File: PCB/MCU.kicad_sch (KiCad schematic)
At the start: 27 parts, among them J1 SWD, SW65 Settings, SW66 Reset, U2 W25Q128JVS, U3 RP2040, Y1 12MHz

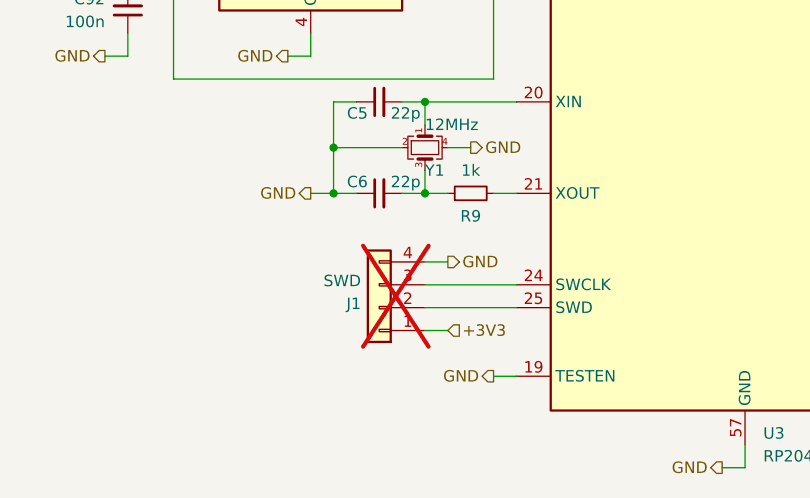
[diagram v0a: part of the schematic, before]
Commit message: Changed RGB LED voltage to 5V.
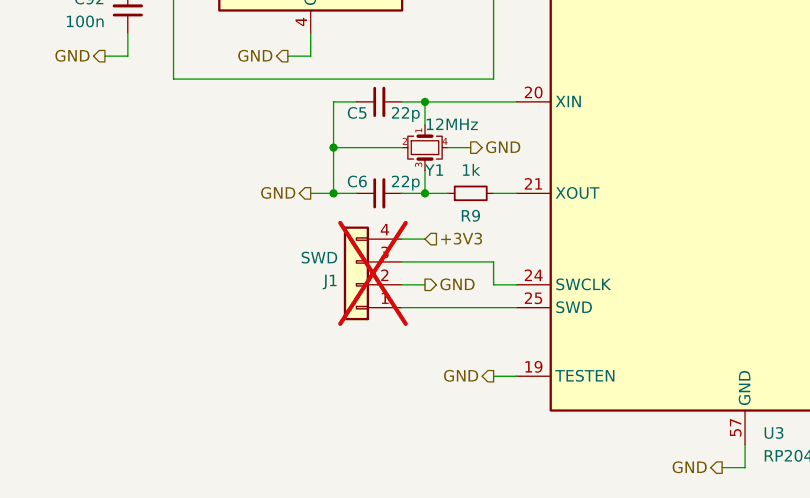
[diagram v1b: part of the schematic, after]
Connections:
- net +3V3: now also J1.4 (Pin_4); no longer J1.1 (Pin_1)
- net GND: now also J1.2 (Pin_2); no longer J1.4 (Pin_4)
- net at U3.25 (SWD): now also J1.1 (Pin_1); no longer J1.2 (Pin_2)
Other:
- moved on the sheet: J1
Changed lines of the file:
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@@
+    (stroke (width 0) (type default))
+  )
+  (wire (pts (xy 66.04 100.33) (xy 68.58 100.33))
     (stroke (width 0) (type default))
   )
@@
     (stroke (width 0) (type default))
   )
+  (wire (pts (xy 66.04 97.79) (xy 66.04 100.33))
+    (stroke (width 0) (type default))
+  )
   (wire (pts (xy 167.64 16.51) (xy 177.8 16.51))
     (stroke (width 0) (type default))
@@
     (stroke (width 0) (type default))
   )
-  (wire (pts (xy 58.42 100.33) (xy 68.58 100.33))
-    (stroke (width 0) (type default))
-  )
   (wire (pts (xy 116.84 26.67) (xy 106.68 26.67))
     (stroke (width 0) (type default))
@@
     (stroke (width 0) (type default))
   )
+  (wire (pts (xy 55.88 97.79) (xy 66.04 97.79))
+    (stroke (width 0) (type default))
+  )
   (wire (pts (xy 106.68 16.51) (xy 116.84 16.51))
     (stroke (width 0) (type default))
@@
     (stroke (width 0) (type default))
   )
-  (wire (pts (xy 60.96 97.79) (xy 58.42 97.79))
+  (wire (pts (xy 58.42 100.33) (xy 55.88 100.33))
     (stroke (width 0) (type default))
   )
@@
     (stroke (width 0) (type default))
   )
-  (wire (pts (xy 58.42 102.87) (xy 68.58 102.87))
+  (wire (pts (xy 55.88 102.87) (xy 68.58 102.87))
     (stroke (width 0) (type default))
   )
@@
     (stroke (width 0) (type default))
   )
-  (wire (pts (xy 60.96 105.41) (xy 58.42 105.41))
+  (wire (pts (xy 58.42 95.25) (xy 55.88 95.25))
     (stroke (width 0) (type default))
   )
@@
     (effects (font (size 1.27 1.27)) (justify right))
   )
-  (hierarchical_label "+3V3" (shape input) (at 60.96 105.41 0) (fields_autoplaced)
+  (hierarchical_label "+3V3" (shape input) (at 58.42 95.25 0) (fields_autoplaced)
     (effects (font (size 1.27 1.27)) (justify left))
   )
@@
     (effects (font (size 1.27 1.27)) (justify right))
   )
-  (hierarchical_label "GND" (shape output) (at 60.96 97.79 0) (fields_autoplaced)
+  (hierarchical_label "GND" (shape output) (at 58.42 100.33 0) (fields_autoplaced)
     (effects (font (size 1.27 1.27)) (justify left))
   )
@@
     )
   )
-  (symbol (lib_id "Connector_Generic:Conn_01x04") (at 53.34 102.87 180) (unit 1)
-    (in_bom no) (on_board yes) (dnp yes) (fields_autoplaced)
-    (property "Reference" "J1" (at 51.308 102.4347 0)
+  (symbol (lib_id "Connector_Generic:Conn_01x04") (at 50.8 100.33 180) (unit 1)
+    (in_bom no) (on_board yes) (dnp yes)
+    (property "Reference" "J1" (at 48.768 99.8947 0)
       (effects (font (size 1.27 1.27)) (justify left))
     )
-    (property "Value" "SWD" (at 51.308 99.8978 0)
+    (property "Value" "SWD" (at 48.768 97.3578 0)
       (effects (font (size 1.27 1.27)) (justify left))
     )
-    (property "Footprint" "Connector_PinHeader_2.54mm:PinHeader_1x04_P2.54mm_Vertical" (at 53.34 102.87 0)
-      (effects (font (size 1.27 1.27)) hide)
-    )
-    (property "Datasheet" "~" (at 53.34 102.87 0)
-      (effects (font (size 1.27 1.27)) hide)
-    )
-    (property "Description" "Debug header" (at 53.34 102.87 0)
-      (effects (font (size 1.27 1.27)) hide)
-    )
+    (property "Footprint" "Connector_PinHeader_2.54mm:PinHeader_1x04_P2.54mm_Vertical" (at 50.8 100.33 0)
+      (effects (font (size 1.27 1.27)) hide)
+    )
+    (property "Datasheet" "~" (at 50.8 100.33 0)
+      (effects (font (size 1.27 1.27)) hide)
+    )
+    (property "Description" "Debug header" (at 50.8 100.33 0)
+      (effects (font (size 1.27 1.27)) hide)
+    )

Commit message: Massive mistake corrections and clarifications.
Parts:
- added R10: 10k, Resistor_SMD:R_0402_1005Metric, symbol Device:R_Small
- R7, R8: value 22 -> 27; LCSC part number C25092 -> C25100
- SW65: value Settings -> USB Boot
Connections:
- net +3V3: now also R10.2
- net at SW66.2 (B), U3.26 (RUN): now also R10.1
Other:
- moved on the sheet: C10, C11, C12, C13, C14, C15, C16, C17, C18, C19, C5, C6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

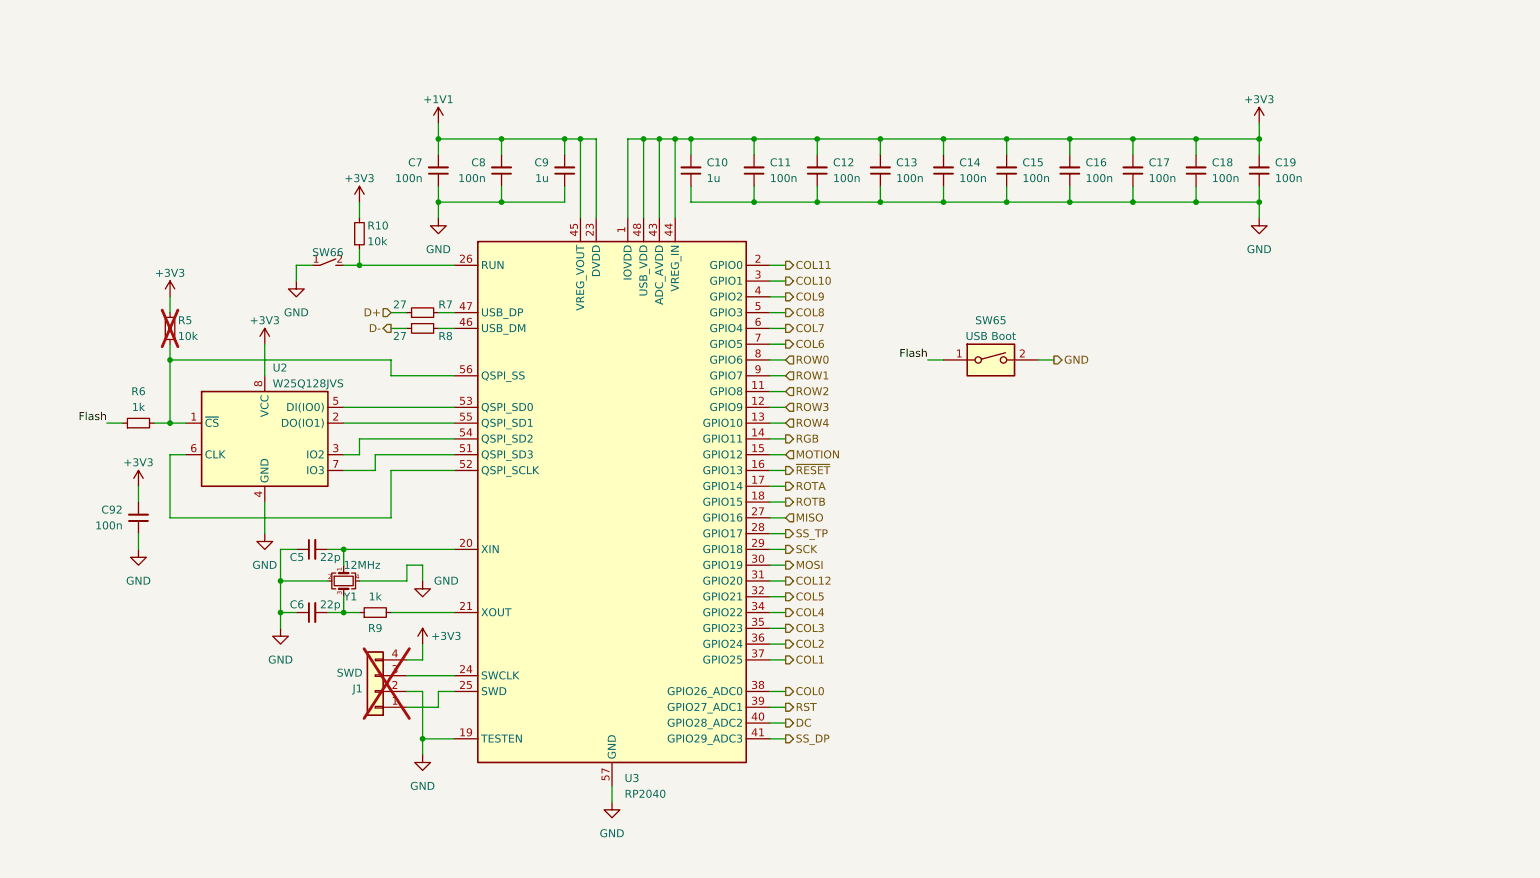
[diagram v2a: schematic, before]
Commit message: Fixed error in MCU sheet. Changed flash symbol to the one used in Kicad 7.
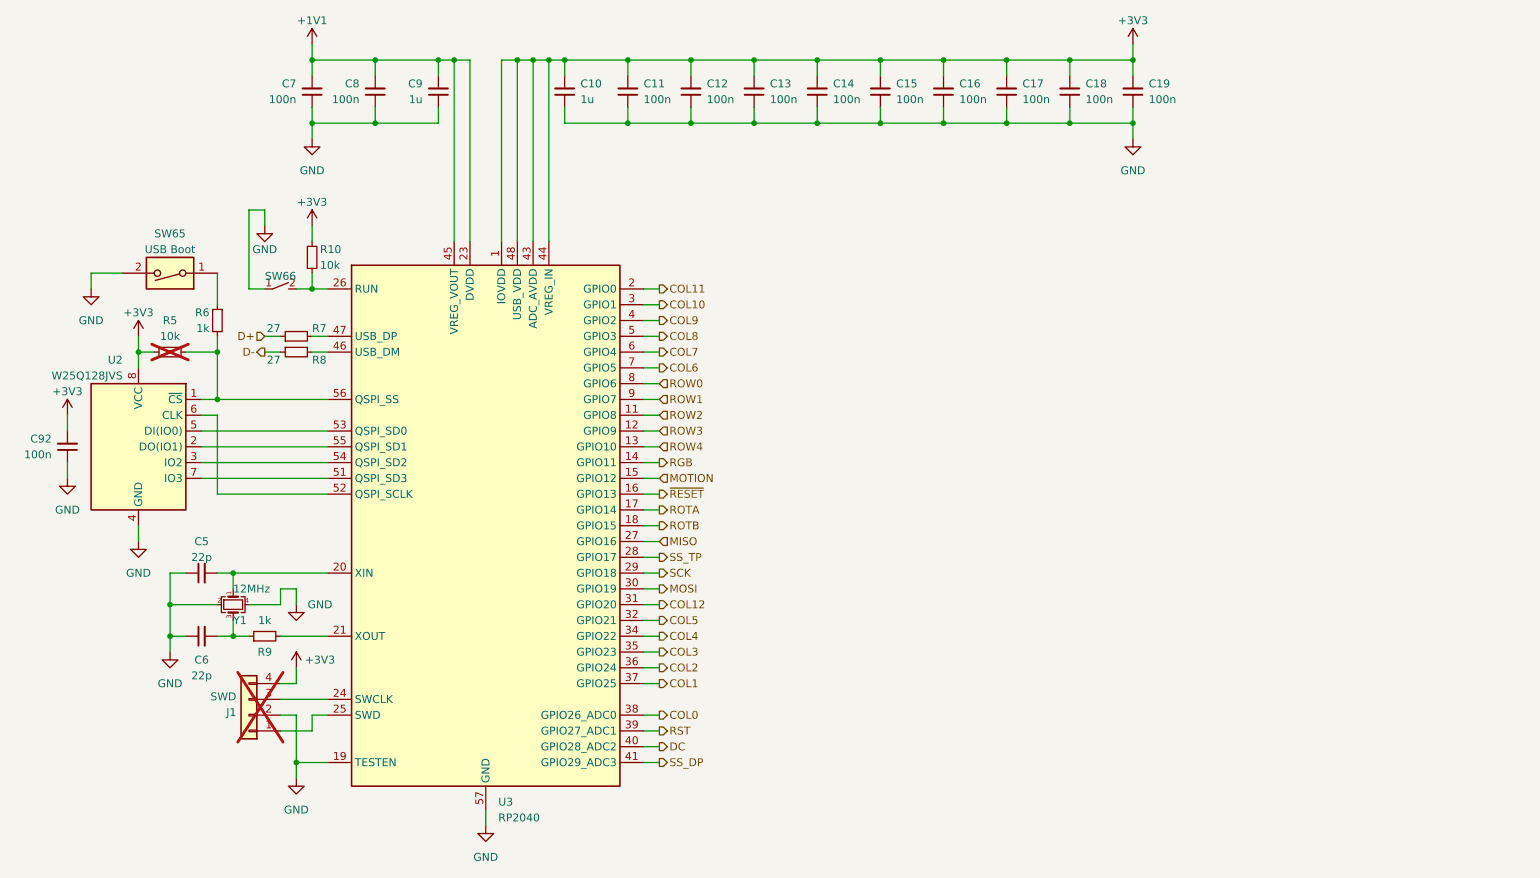
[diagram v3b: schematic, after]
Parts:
- U2: footprint Package_SO:SOIC-8_5.275x5.275mm_P1.27mm -> Package_SO:SOIC-8_5.23x5.23mm_P1.27mm; LCSC part number C97521 -> (none)
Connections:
- net Flash: no longer names the net of R6.1, SW65.1
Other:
- moved on the sheet: C10, C11, C12, C13, C14, C15, C16, C17, C18, C19, C5, C6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

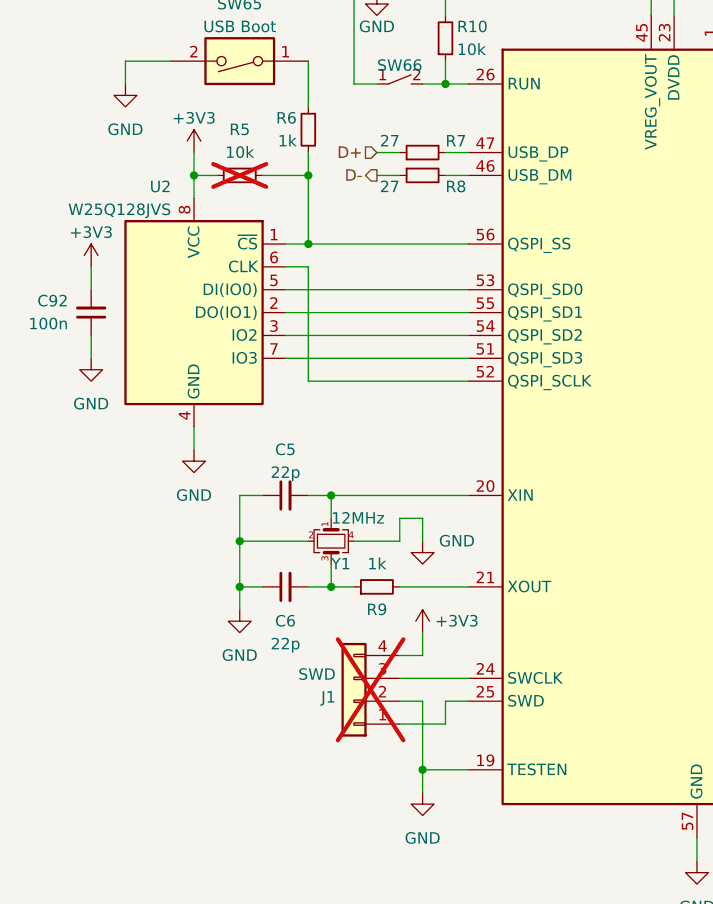
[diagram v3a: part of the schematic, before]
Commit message: Rewording of readme. Added files for JLC PCBA. Changed USB C connector and moved it away from board.
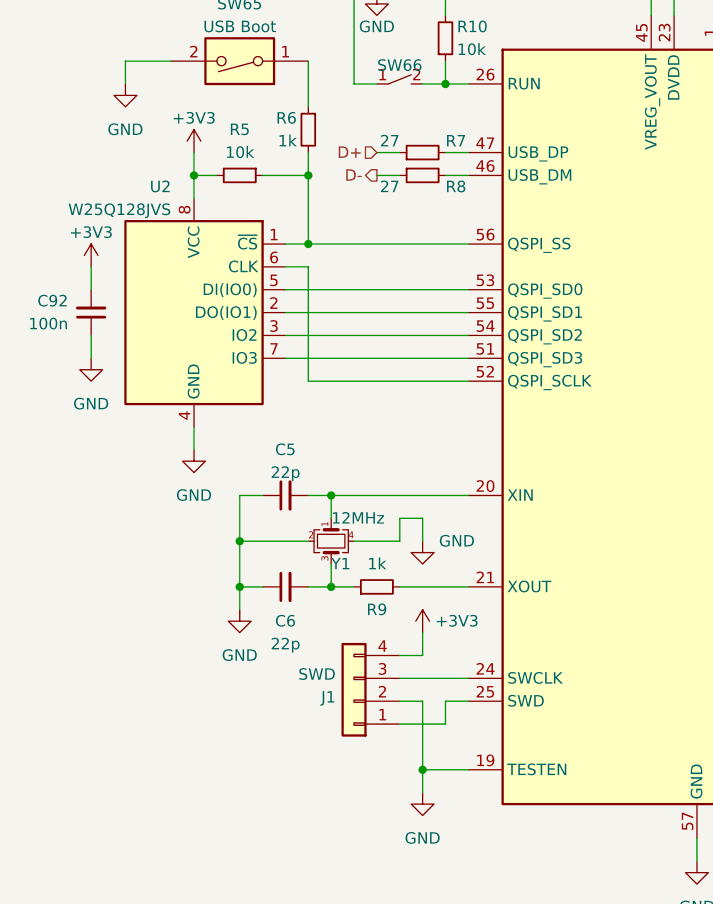
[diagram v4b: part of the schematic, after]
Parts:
- C10, C9: LCSC (none) -> C15849; LCSC part number C15849 -> (none)
- C11, C12, C13, C14, C15, C16, C17, C18, C19, C7, C8, C92: LCSC (none) -> C1525; LCSC part number C1525 -> (none)
- C5, C6: LCSC (none) -> C1555; LCSC part number C1555 -> (none)
- J1: now fitted
- R10: LCSC (none) -> C25744; LCSC part number C25744 -> (none)
- R5: LCSC (none) -> C25744; LCSC part number C25744 -> (none); now fitted
- R6, R9: LCSC (none) -> C11702; LCSC part number C11702 -> (none)
- R7, R8: LCSC (none) -> C25100; LCSC part number C25100 -> (none)
- SW65: footprint Button_Switch_SMD:SW_DIP_SPSTx01_Slide_Copal_CHS-01B_W7.62mm_P1.27mm -> Button_Switch_SMD:SW_DIP_SPSTx01_Slide_6.7x4.1mm_W8.61mm_P2.54mm_LowProfile; LCSC (none) -> C600988; LCSC part number C40735 -> (none)
- SW66: LCSC (none) -> C318884; LCSC part number C318884 -> (none)
- U2: LCSC (none) -> C97521
- U3: LCSC (none) -> C2040; LCSC part number C2040 -> (none)
- Y1: LCSC (none) -> C9002; LCSC part number C9002 -> (none)
